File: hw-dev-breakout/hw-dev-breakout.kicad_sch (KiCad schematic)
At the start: 21 parts, among them J101 CN7, J102 CN10, SW101 SW_Push, U101 TCAN332, U102 TCAN332, U103 TCAN332

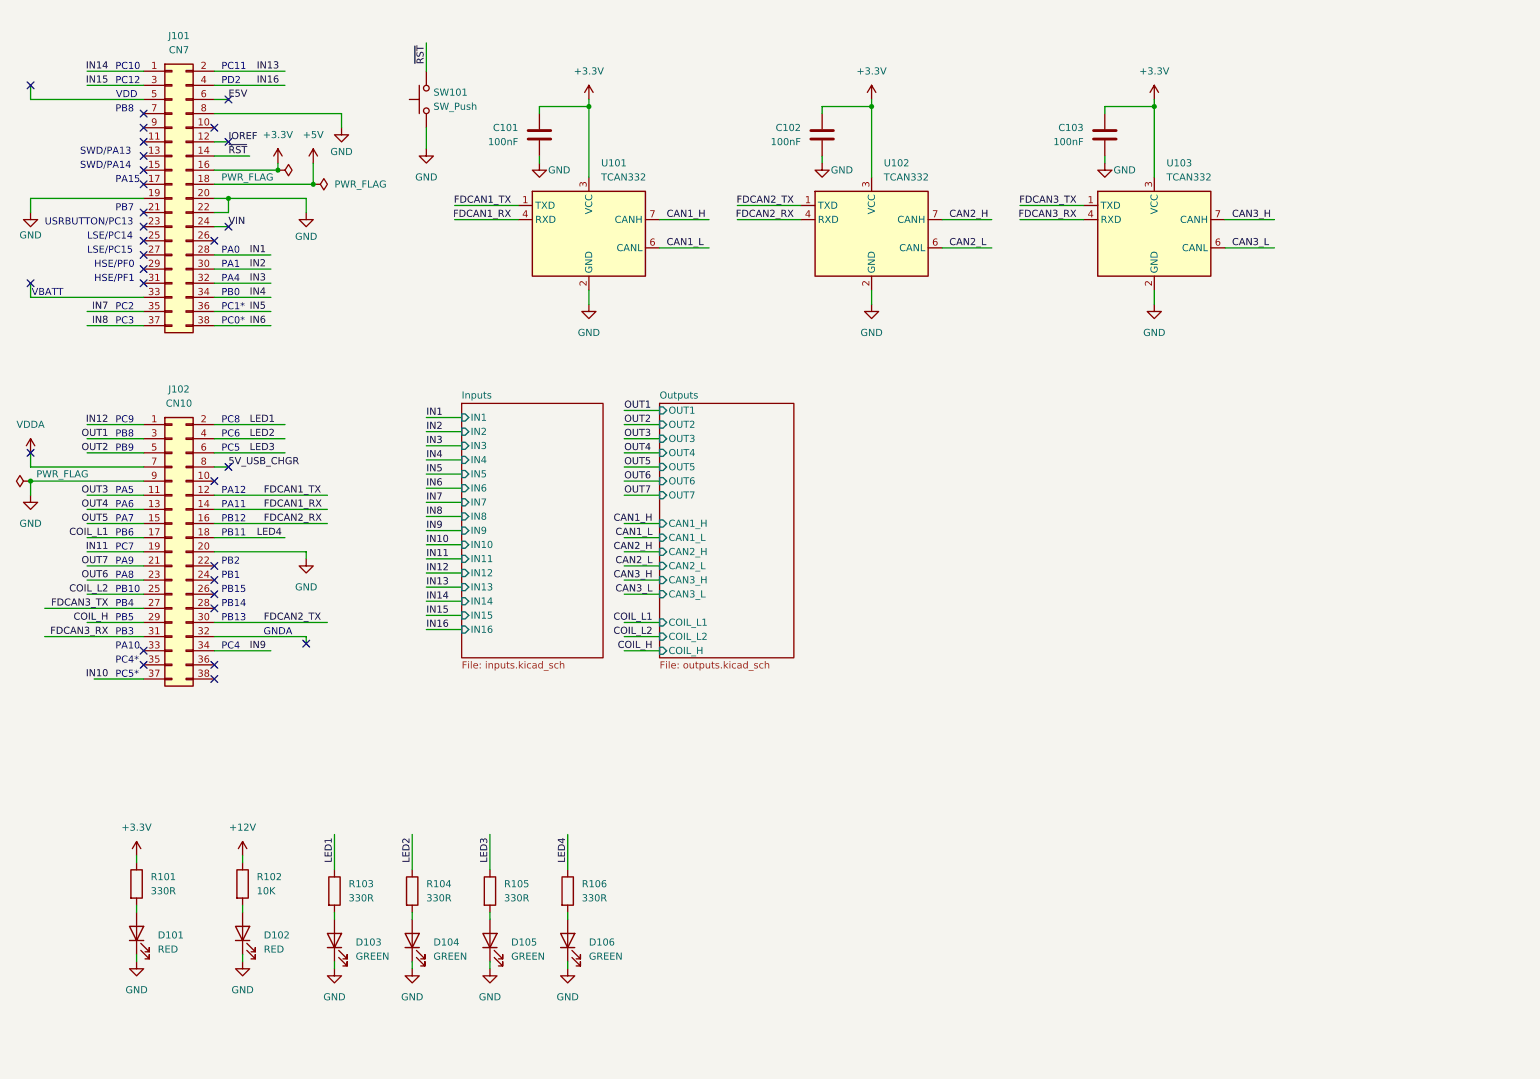
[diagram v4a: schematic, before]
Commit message: pcb: Partially routed
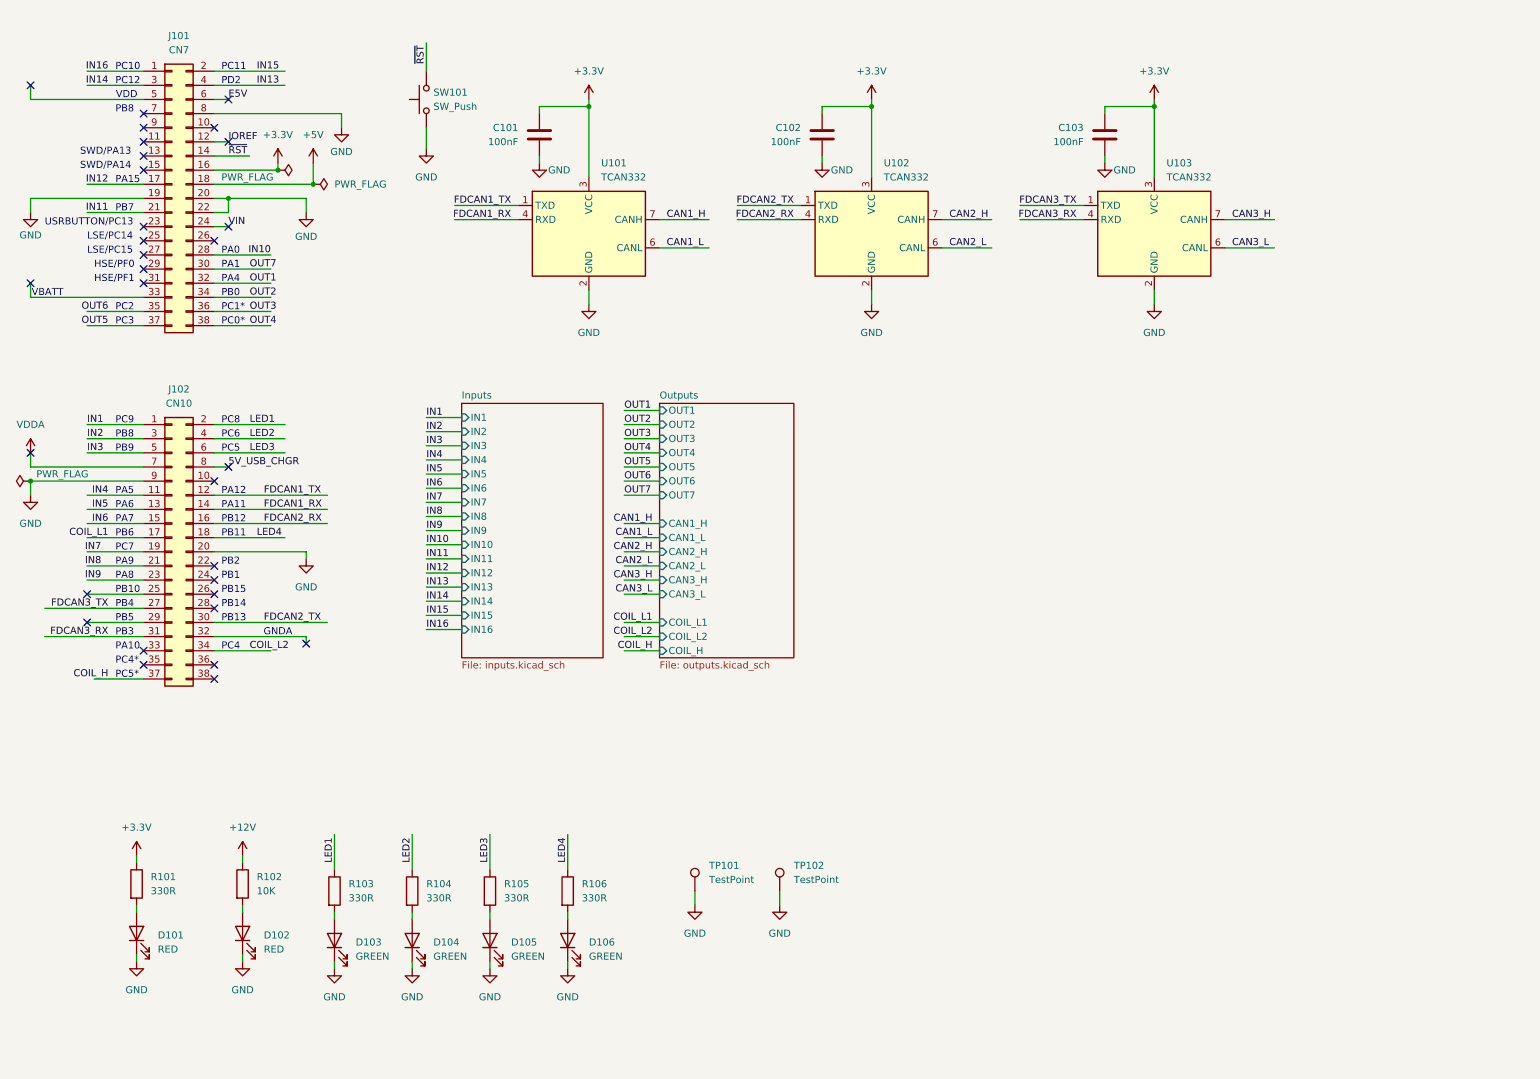
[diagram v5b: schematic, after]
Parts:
- added TP101, TP102: TestPoint, TestPoint:TestPoint_Pad_4.0x4.0mm, symbol Connector:TestPoint
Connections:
- net COIL_H: now also J102.37 (Pin_37); no longer J102.29 (Pin_29)
- net COIL_L2: now also J102.34 (Pin_34); no longer J102.25 (Pin_25)
- net GND: now also TP101.1, TP102.1
- net IN1: now also J102.1 (Pin_1); no longer J101.28 (Pin_28)
- net IN10: now also J101.28 (Pin_28); no longer J102.37 (Pin_37)
- net IN11: now also J101.21 (Pin_21); no longer J102.19 (Pin_19)
- net IN12: now also J101.17 (Pin_17); no longer J102.1 (Pin_1)
- net IN13: now also J101.4 (Pin_4); no longer J101.2 (Pin_2)
- net IN14: now also J101.3 (Pin_3); no longer J101.1 (Pin_1)
- net IN15: now also J101.2 (Pin_2); no longer J101.3 (Pin_3)
- net IN16: now also J101.1 (Pin_1); no longer J101.4 (Pin_4)
- net IN2: now also J102.3 (Pin_3); no longer J101.30 (Pin_30)
- net IN3: now also J102.5 (Pin_5); no longer J101.32 (Pin_32)
- net IN4: now also J102.11 (Pin_11); no longer J101.34 (Pin_34)
- net IN5: now also J102.13 (Pin_13); no longer J101.36 (Pin_36)
- net IN6: now also J102.15 (Pin_15); no longer J101.38 (Pin_38)
- net IN7: now also J102.19 (Pin_19); no longer J101.35 (Pin_35)
- net IN8: now also J102.21 (Pin_21); no longer J101.37 (Pin_37)
- net IN9: now also J102.23 (Pin_23); no longer J102.34 (Pin_34)
- net OUT1: now also J101.32 (Pin_32); no longer J102.3 (Pin_3)
- net OUT2: now also J101.34 (Pin_34); no longer J102.5 (Pin_5)
- net OUT3: now also J101.36 (Pin_36); no longer J102.11 (Pin_11)
- net OUT4: now also J101.38 (Pin_38); no longer J102.13 (Pin_13)
- net OUT5: now also J101.37 (Pin_37); no longer J102.15 (Pin_15)
- net OUT6: now also J101.35 (Pin_35); no longer J102.23 (Pin_23)
- net OUT7: now also J101.30 (Pin_30); no longer J102.21 (Pin_21)

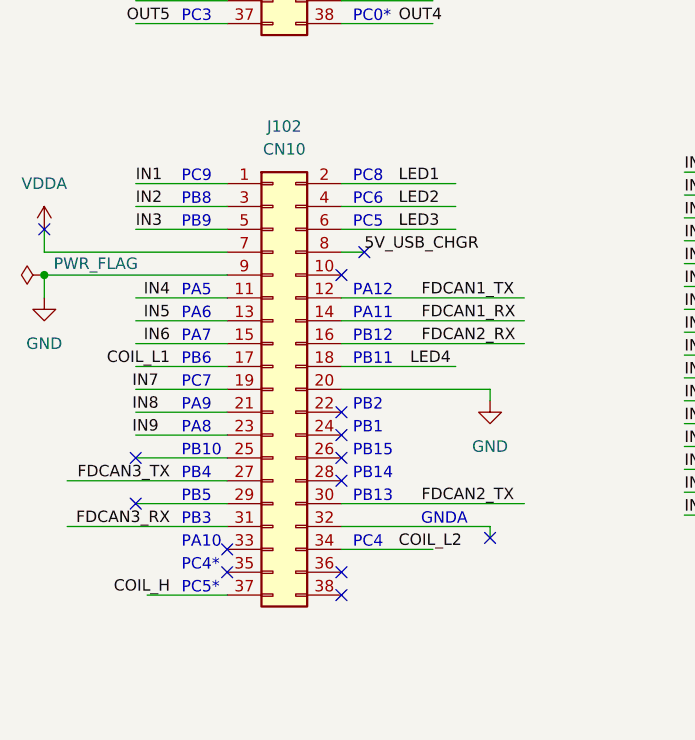
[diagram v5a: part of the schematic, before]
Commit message: pcb: Routed, using jlc 4 layer specs
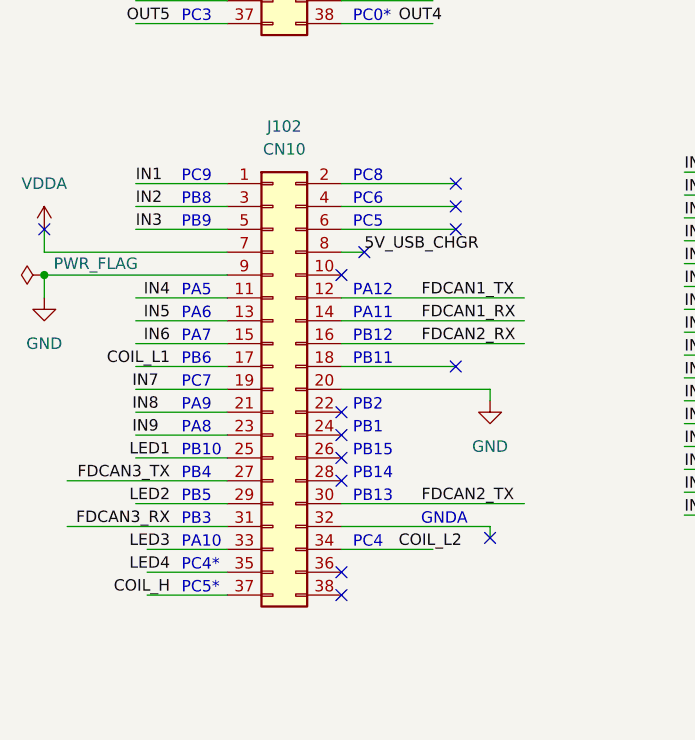
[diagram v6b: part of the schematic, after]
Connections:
- net LED1: now also J102.25 (Pin_25); no longer J102.2 (Pin_2)
- net LED2: now also J102.29 (Pin_29); no longer J102.4 (Pin_4)
- net LED3: now also J102.33 (Pin_33); no longer J102.6 (Pin_6)
- net LED4: now also J102.35 (Pin_35); no longer J102.18 (Pin_18)
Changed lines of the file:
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@@
-	)
-	(no_connect
-		(at 25.4 116.84)
 	)
 	(no_connect
@@
 	)
 	(no_connect
+		(at 60.96 88.9)
+	)
+	(no_connect
 		(at 35.56 60.96)
 	)
@@
 	)
 	(no_connect
+		(at 60.96 91.44)
+	)
+	(no_connect
 		(at 48.26 132.08)
 	)
@@
 	)
 	(no_connect
+		(at 60.96 106.68)
+	)
+	(no_connect
 		(at 48.26 119.38)
 	)
 	(no_connect
-		(at 35.56 129.54)
+		(at 60.96 86.36)
 	)
 	(no_connect
@@
 	)
 	(no_connect
-		(at 25.4 121.92)
-	)
-	(no_connect
 		(at 35.56 33.02)
-	)
-	(no_connect
-		(at 35.56 127)
 	)
 	(no_connect
@@
 	(wire
 		(pts
+			(xy 26.67 127) (xy 35.56 127)
+		)
+		(stroke
+			(width 0)
+			(type default)
+		)
+	)
+	(wire
+		(pts
 			(xy 25.4 91.44) (xy 35.56 91.44)
 		)
@@
 		(pts
 			(xy 142.24 46.99) (xy 153.67 46.99)
+		)
+		(stroke
+			(width 0)
+			(type default)
+		)
+	)
+	(wire
+		(pts
+			(xy 26.67 129.54) (xy 35.56 129.54)
 		)
 		(stroke
@@
 	)
 	(label "LED3"
-		(at 54.61 91.44 0)
-		(fields_autoplaced yes)
-		(effects
-			(font
-				(size 1.27 1.27)
-			)
-			(justify left bottom)
+		(at 29.21 127 180)
+		(fields_autoplaced yes)
+		(effects
+			(font
+				(size 1.27 1.27)
+			)
+			(justify right bottom)
 		)
 	)
@@
 	)
 	(label "LED1"
-		(at 54.61 86.36 0)
-		(fields_autoplaced yes)
-		(effects
-			(font
-				(size 1.27 1.27)
-			)
-			(justify left bottom)
+		(at 29.21 116.84 180)
+		(fields_autoplaced yes)
+		(effects
+			(font
+				(size 1.27 1.27)
+			)
+			(justify right bottom)
 		)
 	)
@@
 	)
 	(label "LED4"
-		(at 55.88 106.68 0)
-		(fields_autoplaced yes)
-		(effects
-			(font
-				(size 1.27 1.27)
-			)
-			(justify left bottom)
+		(at 29.21 129.54 180)
+		(fields_autoplaced yes)
+		(effects
+			(font
+				(size 1.27 1.27)
+			)
+			(justify right bottom)
 		)
 	)
@@
 	)
 	(label "LED2"
-		(at 54.61 88.9 0)
-		(fields_autoplaced yes)
-		(effects
-			(font
-				(size 1.27 1.27)
-			)
-			(justify left bottom)
-		)
-	)
+		(at 29.21 121.92 180)
+		(fields_autoplaced yes)
+		(effects
+			(font
+				(size 1.27 1.27)
+			)
+			(justify right bottom)
+		)
+	)

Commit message: pcb: Routed for 2 layer, fixed P-fet error
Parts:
- added C104, C105, C106, C107, C108: 1uF 50V, Capacitor_SMD:C_1206_3216Metric, symbol Device:C
- added F101: 12H1100C 1A, Fuse:Fuse_1206_3216Metric, symbol Device:Fuse
- added U104: L7805, Package_TO_SOT_SMD:TO-252-2, symbol Regulator_Linear:L7805
- TP101, TP102: footprint TestPoint:TestPoint_Pad_4.0x4.0mm -> hw-dev-breakout:TestPoint_Pad_4.0x4.0mm
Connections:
- net +12V: now also C105.1, C106.1, C108.1, U104.1 (IN)
- net +5V: now also C104.1
- net E5V: now also F101.2
- net GND: now also C104.2, C105.2, C106.2, C107.2, C108.2, U104.2 (GND)
- new net 5V_REGOUT: C107.1, F101.1, U104.3 (OUT)
- no-connect marks 31 -> 30
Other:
- note added: "Optional Nucleo Power (E5V Jumper Setting)"

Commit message: Final cleanups for initial fab run
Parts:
- C101, C102, C103: LCSC Part # (none) -> C14663
- C104, C105, C106, C107, C108: LCSC Part # (none) -> C1848
- D101, D102: value RED -> LED_RED; LCSC Part # (none) -> C2286
- D103, D104, D105, D106: value GREEN -> LED_GREEN; footprint LED_SMD:LED_0603_1608Metric -> LED_SMD:LED_0805_2012Metric; LCSC Part # (none) -> C2297
- F101: LCSC Part # (none) -> C182308
- J101, J102: LCSC Part # (none) -> C18905898
- R101, R103, R104, R105, R106: LCSC Part # (none) -> C23138
- R102: LCSC Part # (none) -> C25804
- SW101: LCSC Part # (none) -> C2889015
- TP101, TP102: now not fitted
- U101, U102, U103: value TCAN332 -> SN65HVD232DR; LCSC Part # (none) -> C30530
- U104: LCSC Part # (none) -> C58069
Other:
- note added: "Note: Selected non-FD speed rated CAN transceivers for ease of JLC assembly, but these are pin compatible with TCAN332G (which can do 5Mbps) if needed."
